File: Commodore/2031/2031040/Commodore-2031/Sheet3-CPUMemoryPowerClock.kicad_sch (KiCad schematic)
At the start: 45 parts, among them U1 74LS42, Y1 16MHz

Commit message: Capture sheet 4
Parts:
- renumbered UC2 to UC4
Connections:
- net +5V: now also UB3.18 (VCC), UC3.18 (VCC), UD3.18 (VCC), UE3.18 (VCC)
- net GND: now also UB3.9 (GND), UC3.9 (GND), UD3.9 (GND), UE3.9 (GND)
- net 16MHz renamed 16MHZ
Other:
- moved on the sheet: UC3, UE3

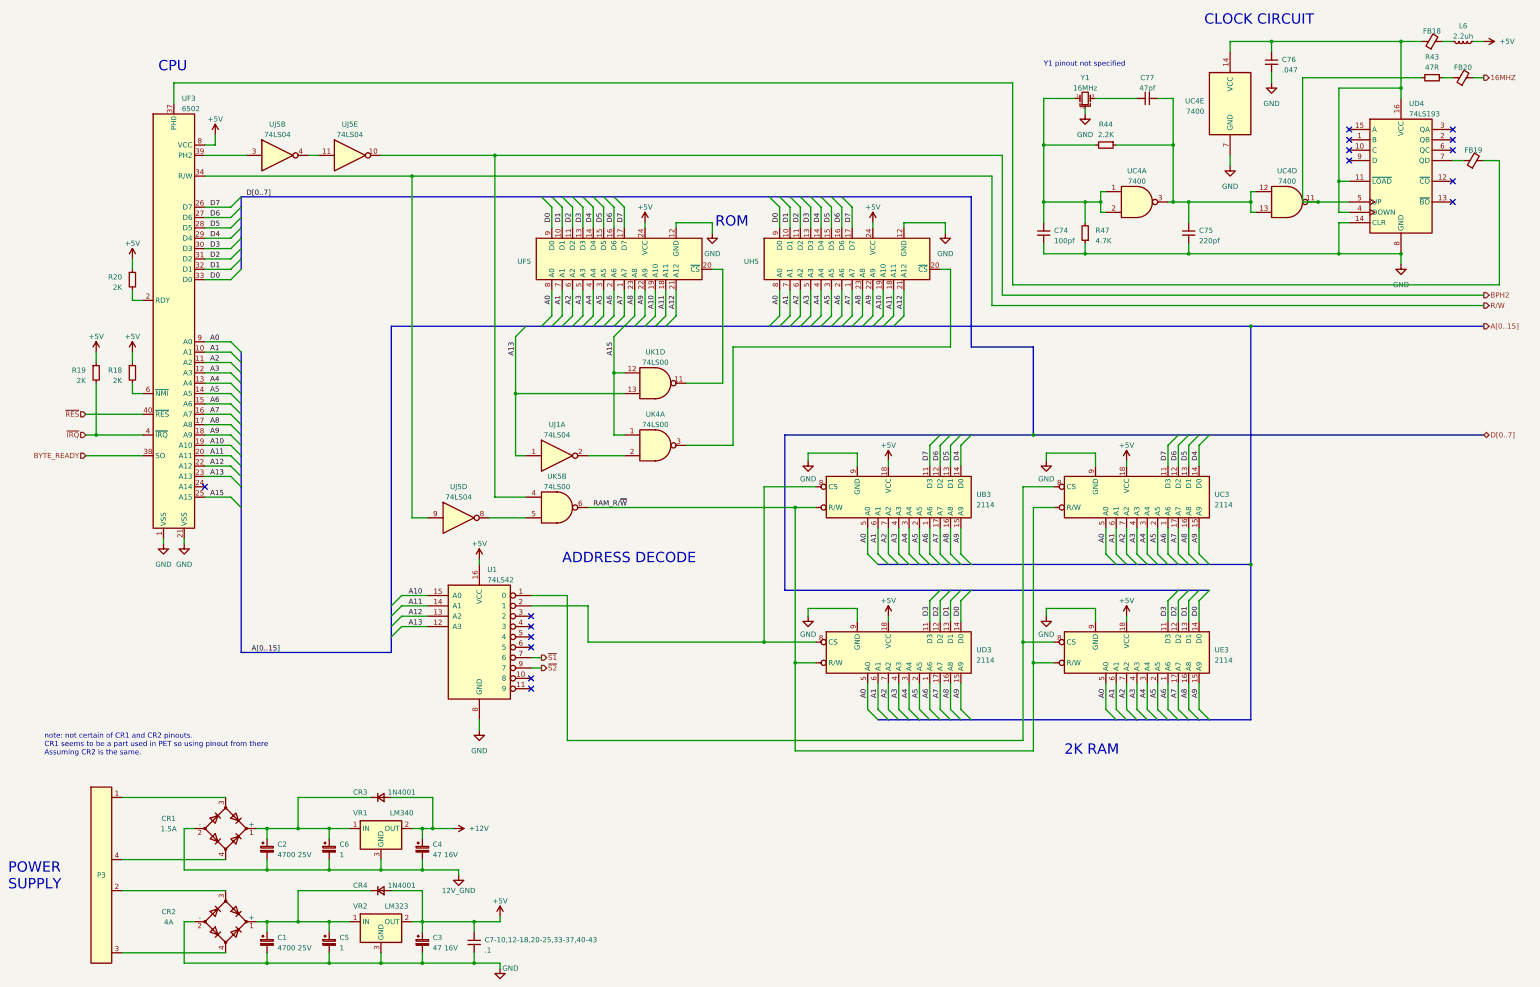
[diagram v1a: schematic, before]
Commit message: Work towards ERC
- Add power flags
- Try to make sense of ground symbols
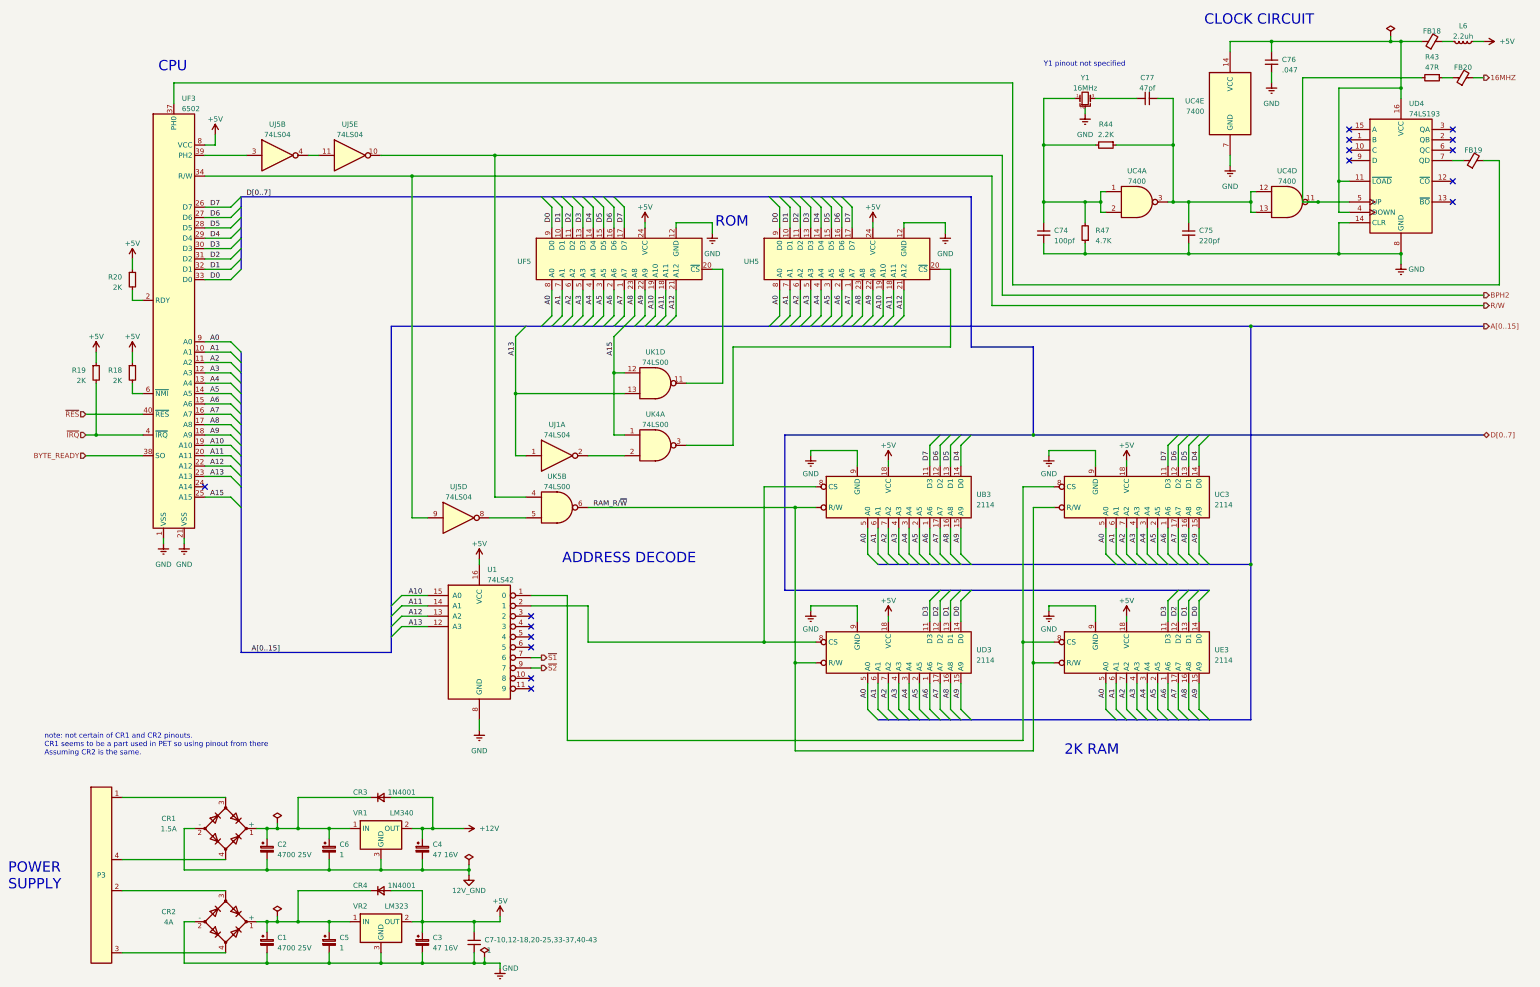
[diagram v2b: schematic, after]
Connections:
- net GND renamed Earth

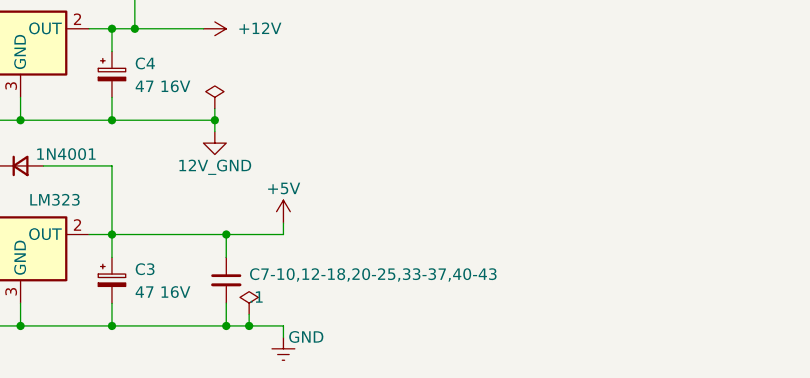
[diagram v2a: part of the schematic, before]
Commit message: Place capacitors and power units
Almost an error-free ERC!
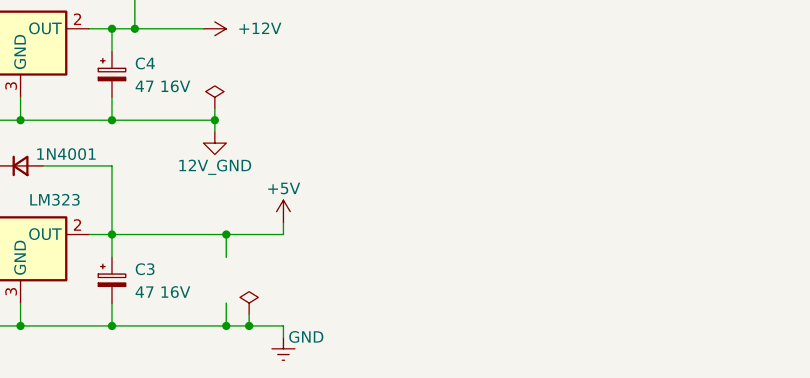
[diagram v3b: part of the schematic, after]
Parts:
- removed C7-10,12-18,20-25,33-37,40-43: .1, symbol Device:C_Small
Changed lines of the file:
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@@
-    )
-  )
-  (symbol (lib_id "Device:C_Small") (at 127 269.24 0) (unit 1)
-    (in_bom yes) (on_board yes) (dnp no) (fields_autoplaced)
-    (property "Reference" "C7-10,12-18,20-25,33-37,40-43" (at 129.54 268.6113 0)
-      (effects (font (size 1.27 1.27)) (justify left))
-    )
-    (property "Value" ".1" (at 129.54 271.1513 0)
-      (effects (font (size 1.27 1.27)) (justify left))
-    )
-    (property "Footprint" "" (at 127 269.24 0)
-      (effects (font (size 1.27 1.27)) hide)
-    )
-    (property "Datasheet" "~" (at 127 269.24 0)
-      (effects (font (size 1.27 1.27)) hide)
-    )
-    (pin "1")
-    (pin "2")
-    (instances
-      (project "Commodore-2031"
-        (path "/4559151c-aecb-4a2a-972f-dcb7dcb5a3dc/42848908-bd55-4e39-a607-ce7f74b344c1"
-          (reference "C7-10,12-18,20-25,33-37,40-43") (unit 1)
-        )
-      )
     )
   )

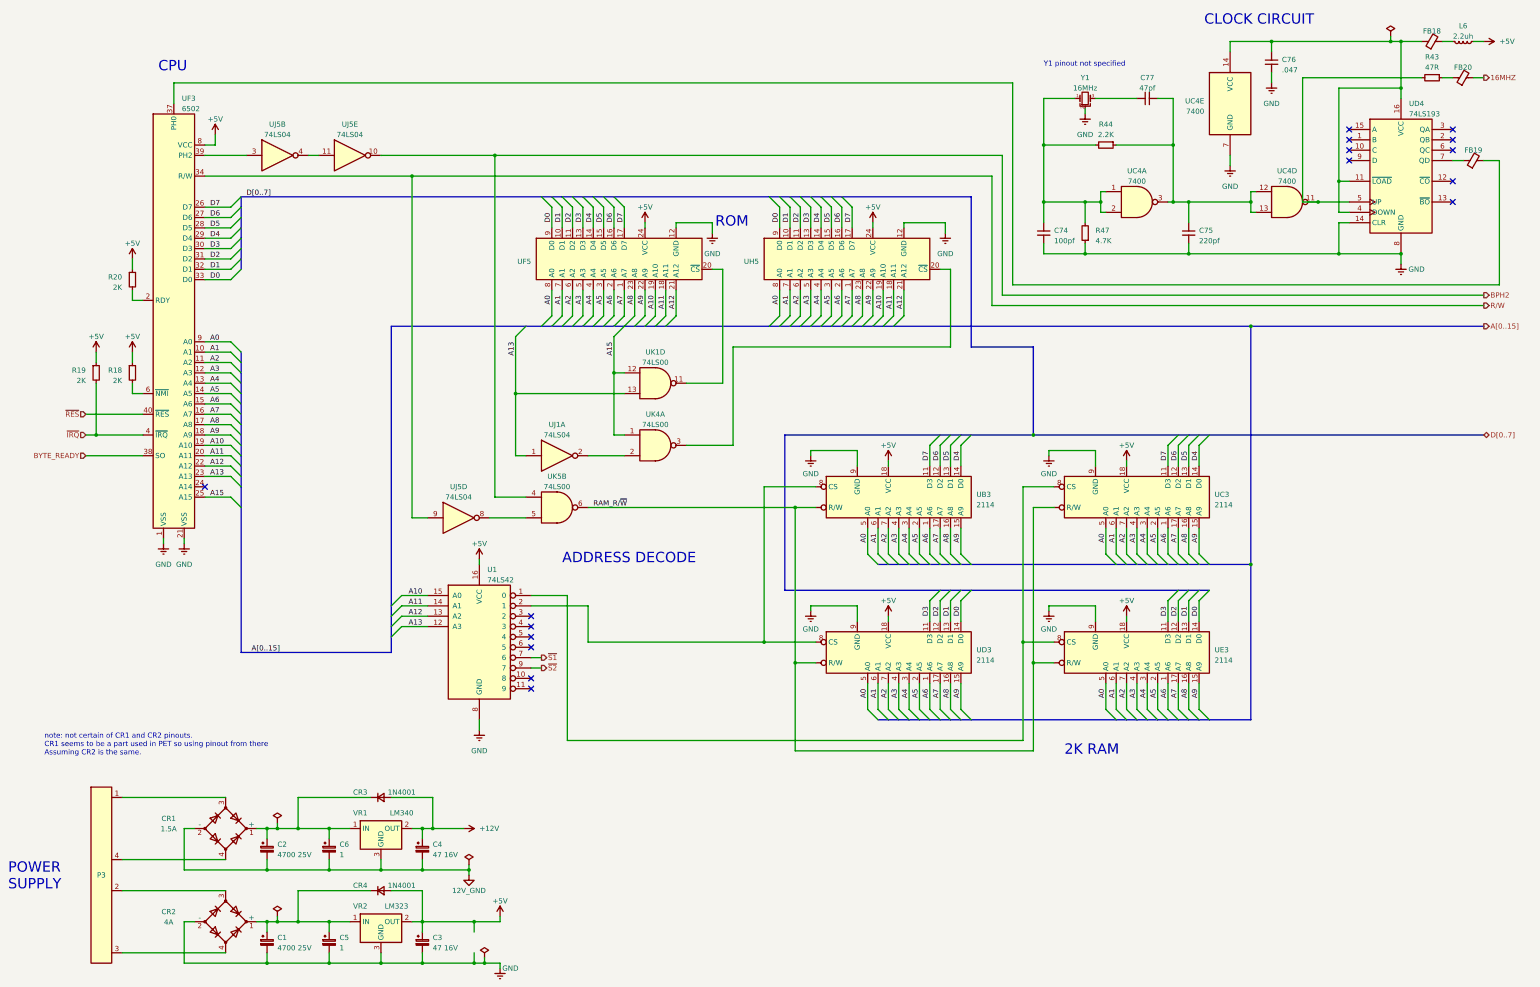
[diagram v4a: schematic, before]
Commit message: Verify schematic against parts list
A few discrepancies appear in original, these are noted in schematic.
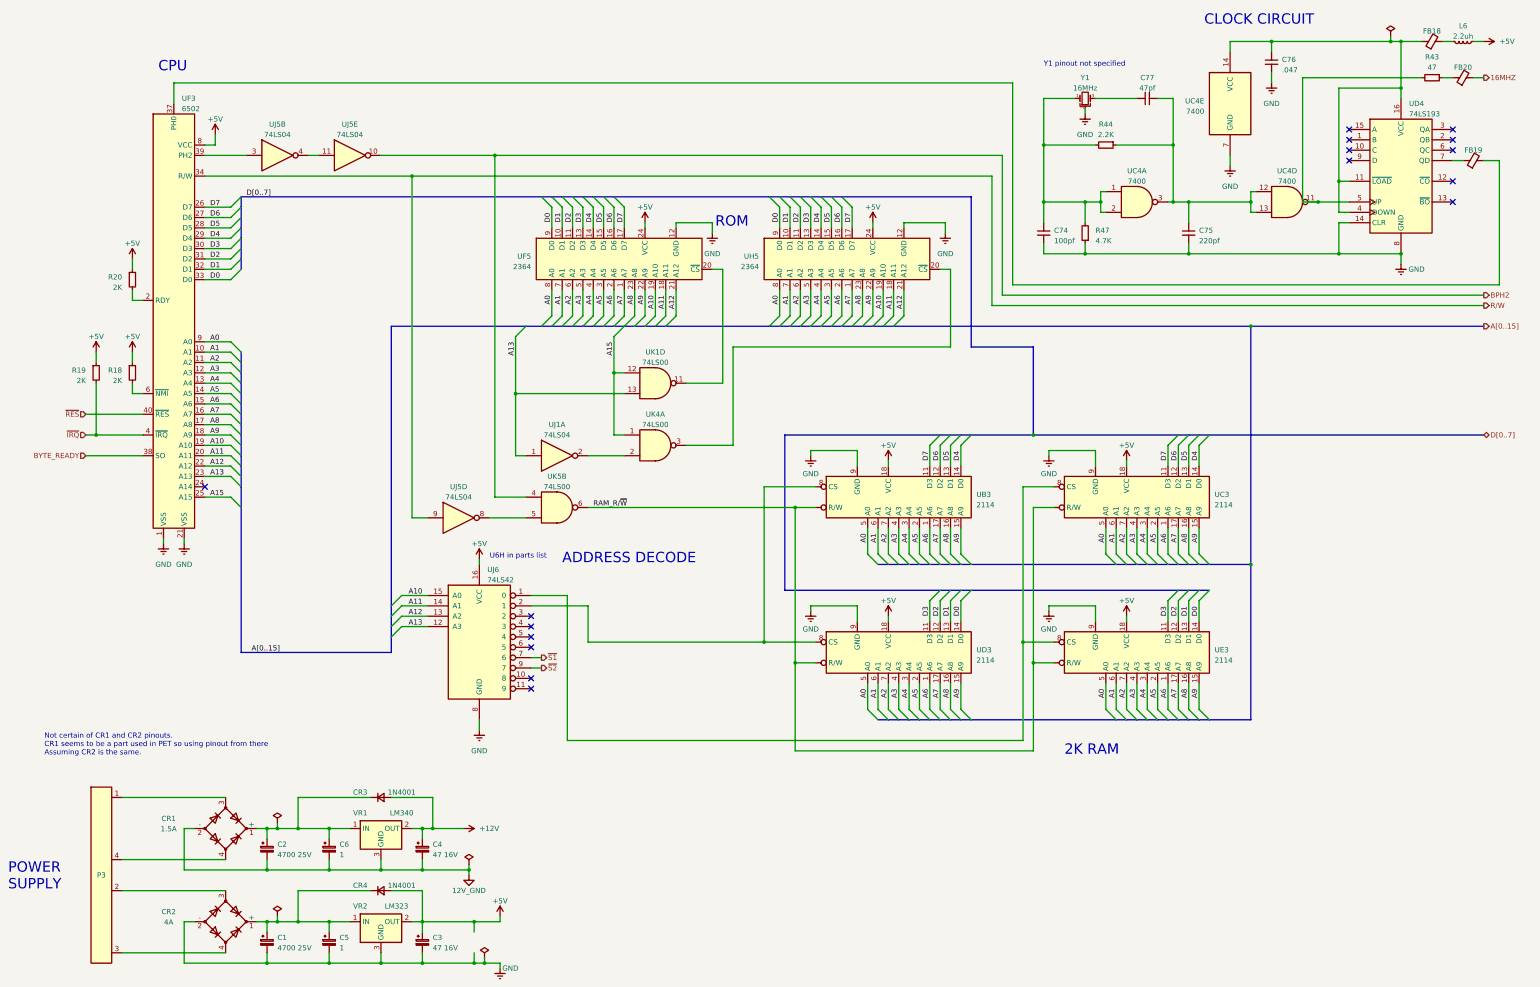
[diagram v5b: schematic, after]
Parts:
- R43: value 47R -> 47
- UF5, UH5: value ~ -> 2364
- renumbered U1 to UJ6
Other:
- note added: "Not certain of CR1 and CR2 pinouts. CR1 seems to be a part used in PET so using pinout from there Assuming CR2 is the same."
- note added: "U6H in parts list"
- note removed: "note: not certain of CR1 and CR2 pinouts. CR1 seems to be a part used in PET so using pinout from there Assuming CR2 is the same."
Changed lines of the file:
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@@
     (effects (font (size 2.54 2.54)) (justify left bottom))
   )
-  (text "note: not certain of CR1 and CR2 pinouts.\nCR1 seems to be a part used in PET so using pinout from there\nAssuming CR2 is the same."
+  (text "Not certain of CR1 and CR2 pinouts.\nCR1 seems to be a part used in PET so using pinout from there\nAssuming CR2 is the same."
     (at 21.59 223.52 0)
     (effects (font (size 1.27 1.27)) (justify left bottom))
@@
   (text "ROM" (at 194.31 93.98 0)
     (effects (font (size 2.54 2.54)) (justify right bottom))
+  )
+  (text "U6H in parts list" (at 130.81 175.26 0)
+    (effects (font (size 1.27 1.27)) (justify left bottom))
   )
   (text "POWER\nSUPPLY" (at 12.7 256.54 0)
@@
       (effects (font (size 1.27 1.27)))
     )
-    (property "Value" "47R" (at 361.95 54.61 90)
+    (property "Value" "47" (at 361.95 54.61 90)
       (effects (font (size 1.27 1.27)))
     )
@@
   (symbol (lib_id "Commodore-2031:2364") (at 163.83 101.6 0) (unit 1)
     (in_bom yes) (on_board yes) (dnp no) (fields_autoplaced)
-    (property "Reference" "UF5" (at 140.97 102.235 0)
+    (property "Reference" "UF5" (at 140.97 100.965 0)
       (effects (font (size 1.27 1.27)) (justify right))
     )
-    (property "Value" "~" (at 154.94 106.68 0)
-      (effects (font (size 1.27 1.27)))
+    (property "Value" "2364" (at 140.97 103.505 0)
+      (effects (font (size 1.27 1.27)) (justify right))
     )
     (property "Footprint" "" (at 154.94 106.68 0)
@@
   (symbol (lib_id "74xx:74LS42") (at 128.27 194.31 0) (unit 1)
     (in_bom yes) (on_board yes) (dnp no) (fields_autoplaced)
-    (property "Reference" "U1" (at 130.2259 177.8 0)
+    (property "Reference" "UJ6" (at 130.2259 177.8 0)
       (effects (font (size 1.27 1.27)) (justify left))
     )
@@
       (project "Commodore-2031"
         (path "/4559151c-aecb-4a2a-972f-dcb7dcb5a3dc/42848908-bd55-4e39-a607-ce7f74b344c1"
-          (reference "U1") (unit 1)
+          (reference "UJ6") (unit 1)
         )
       )
@@
   (symbol (lib_id "Commodore-2031:2364") (at 219.71 101.6 0) (unit 1)
     (in_bom yes) (on_board yes) (dnp no) (fields_autoplaced)
-    (property "Reference" "UH5" (at 196.85 102.235 0)
+    (property "Reference" "UH5" (at 196.85 100.965 0)
       (effects (font (size 1.27 1.27)) (justify right))
     )
-    (property "Value" "~" (at 210.82 106.68 0)
-      (effects (font (size 1.27 1.27)))
+    (property "Value" "2364" (at 196.85 103.505 0)
+      (effects (font (size 1.27 1.27)) (justify right))
     )
     (property "Footprint" "" (at 210.82 106.68 0)
